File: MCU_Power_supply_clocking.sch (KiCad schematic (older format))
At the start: 111 parts, among them U6 STM32H743ZIT6, Y2 NX5032GA-8MHz, Y3 NX3215SA-32.768K-STD-MUA-14

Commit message: Buttons complete
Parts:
- added R?: 47, Resistor_SMD:R_0805_2012Metric_Pad1.20x1.40mm_HandSolder, symbol Device:R
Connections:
- net VDDA: now also R?.2; no longer JP1.1 (A), JP1.1 (A)
- new net: JP1.1 (A), JP1.1 (A), R?.1
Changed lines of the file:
@@
 $Descr A4 11693 8268
 encoding utf-8
-Sheet 5 9
+Sheet 5 10
 Title "Power_and_MCU_clock"
 Date "2021-04-29"
@@
 $EndComp
 Wire Wire Line
-	7680 4080 7890 4080
+	7380 4080 7590 4080
 Wire Wire Line
 	8500 4080 8290 4080
-Text Label 7680 4080 0    50   ~ 0
+Text Label 7380 4080 0    50   ~ 0
 VDDA
 Text Label 8500 4080 2    50   ~ 0
@@
 	1    0    0    -1
 $EndComp
-Text Label 7680 4080 0    50   ~ 0
+Text Label 7380 4080 0    50   ~ 0
 VDDA
 Text Label 8500 4080 2    50   ~ 0
@@
 Wire Wire Line
 	9010 3240 9010 3200
+$Comp
+L Device:R R?
+U 1 1 60D1EBF4
+P 7740 4080
+AR Path="/60D1EBF4" Ref="R?"  Part="1"
+AR Path="/60A03F8A/60D1EBF4" Ref="R?"  Part="1"
+F 0 "R?" V 7650 4080 50  0000 C CNN
+F 1 "47" V 7830 4080 50  0000 C CNN
+F 2 "Resistor_SMD:R_0805_2012Metric_Pad1.20x1.40mm_HandSolder" V 7670 4080 50  0001 C CNN
+F 3 "~" H 7740 4080 50  0001 C CNN
+	1    7740 4080
+	0    1    1    0
+$EndComp
 $EndSCHEMATC

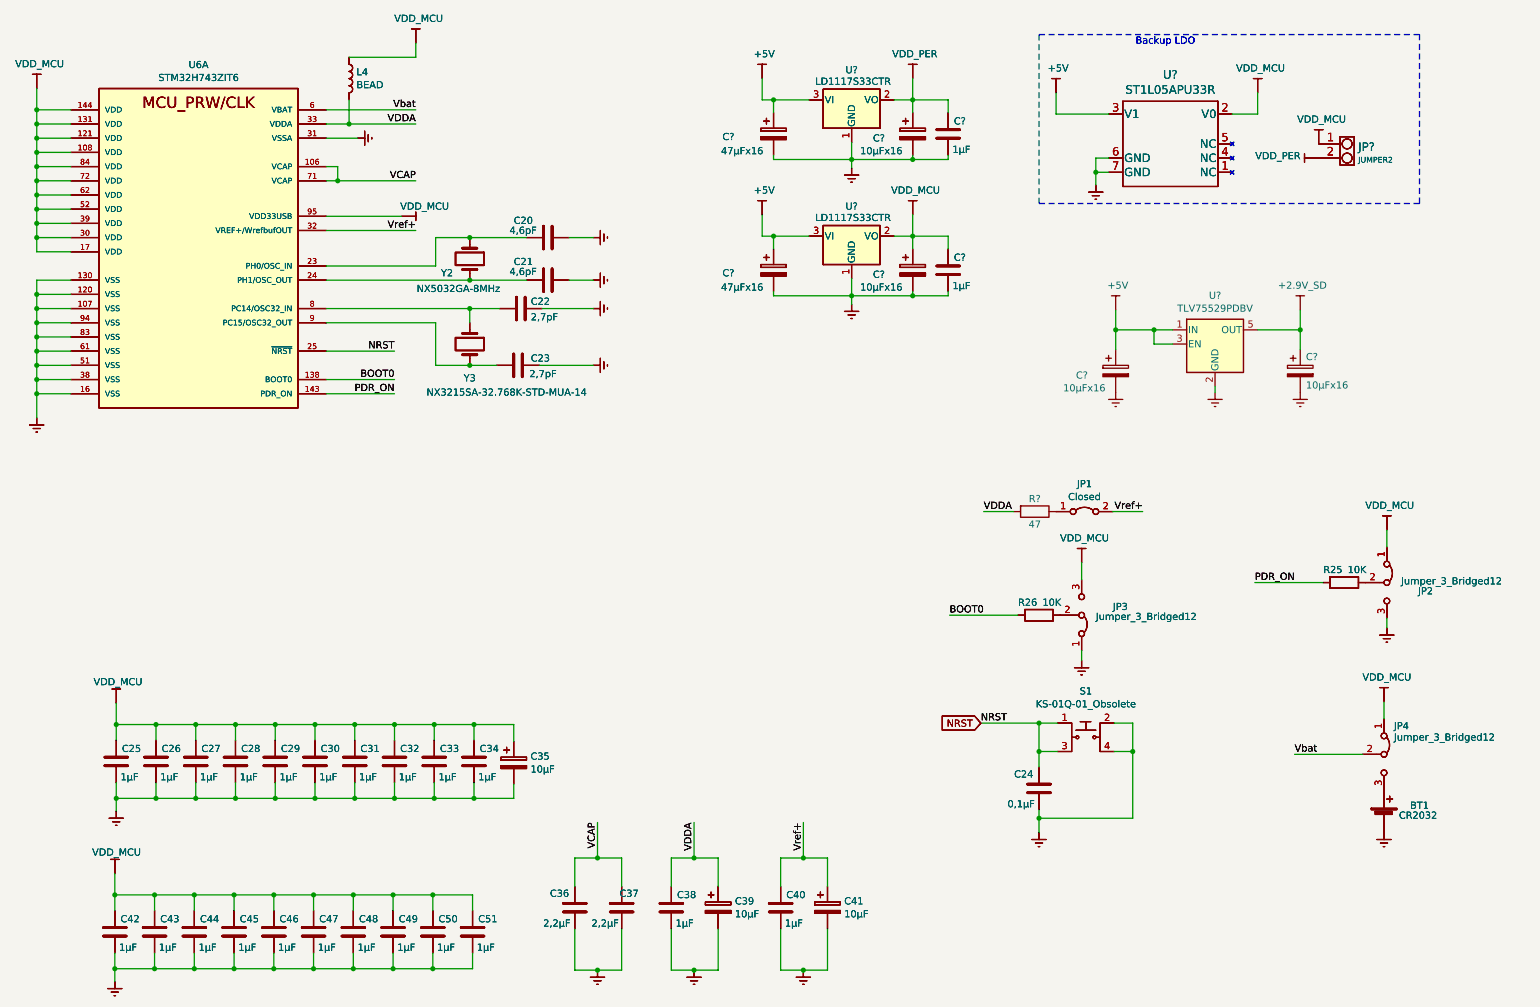
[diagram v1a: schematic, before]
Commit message: delete Main power scheet
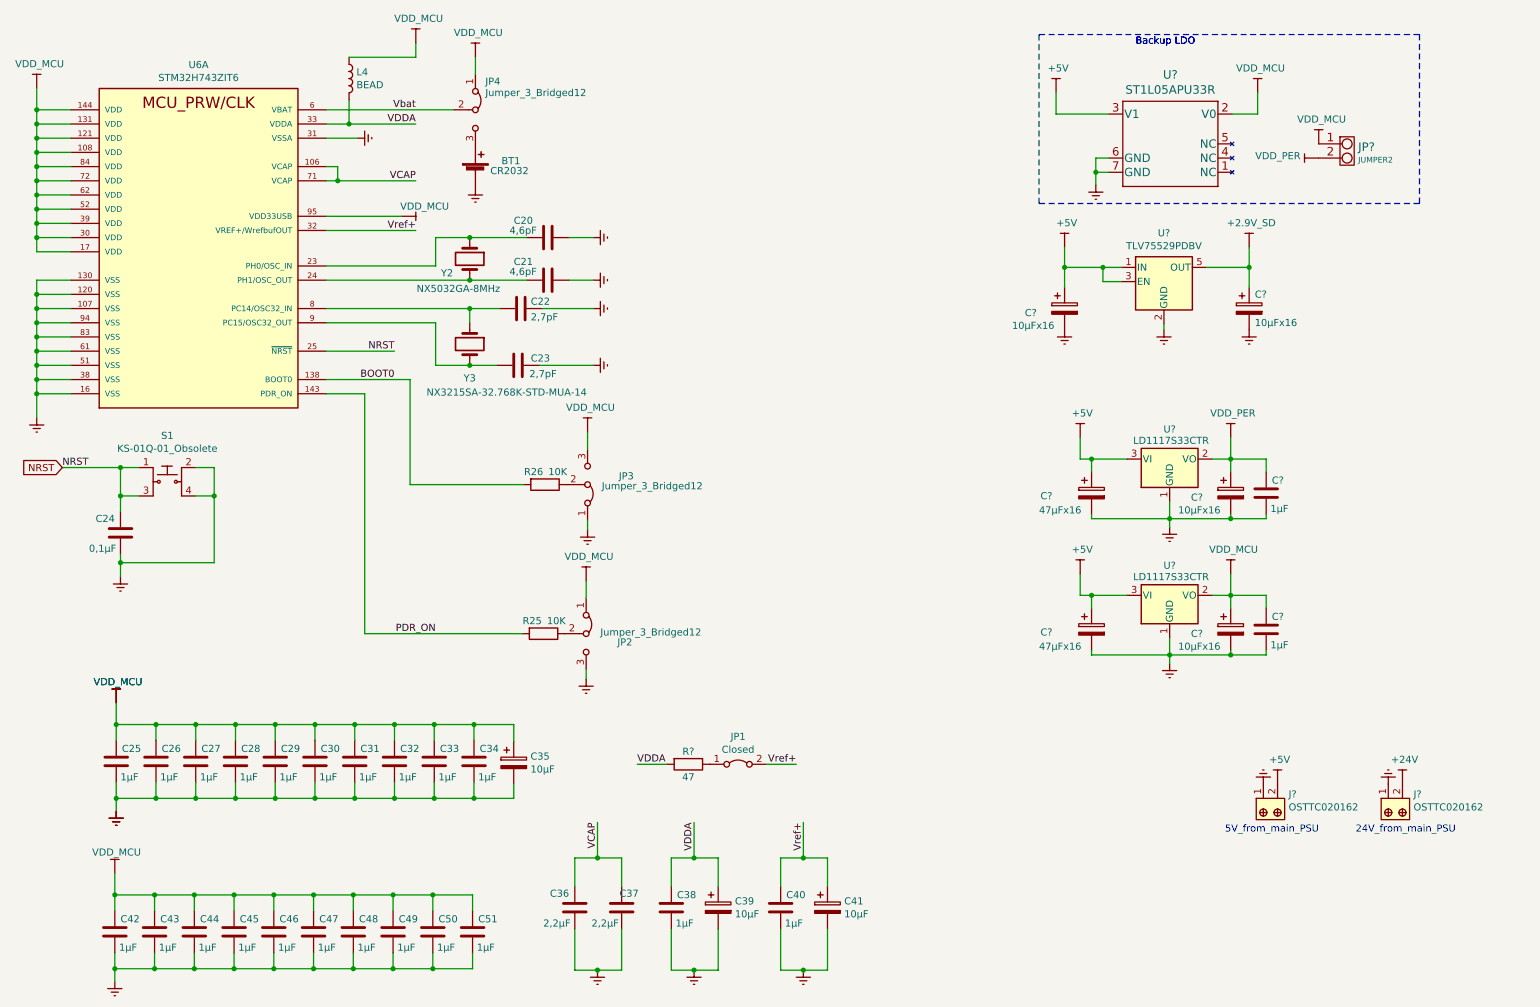
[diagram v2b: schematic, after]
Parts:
- removed BT1: CR2032, symbol Device:Battery_Cell
- removed C20, C21: 4,6pF, Capacitor_SMD:C_0603_1608Metric_Pad1.08x0.95mm_HandSolder, symbol Device:C
- removed C22, C23: 2,7pF, Capacitor_SMD:C_0603_1608Metric_Pad1.08x0.95mm_HandSolder, symbol Device:C
- removed C24: 0,1µF, Capacitor_SMD:C_0805_2012Metric_Pad1.18x1.45mm_HandSolder, symbol Device:C
- removed C25, C26, C27, C28, C29, C30, C31, C32, C33, C34, C38, C40, C42, C43, C44, C45, C46, C47, C48, C49, C50, C51, C? (x2): 1µF, Capacitor_SMD:C_0603_1608Metric_Pad1.08x0.95mm_HandSolder, symbol Device:C
- removed C35, C39, C41: 10µF, Capacitor_Tantalum_SMD:CP_EIA-3216-10_Kemet-I, symbol Device:CP
- removed C36, C37: 2,2µF, Capacitor_SMD:C_0805_2012Metric_Pad1.18x1.45mm_HandSolder, symbol Device:C
- removed C? (x2): 47µFx16, Capacitor_Tantalum_SMD:CP_EIA-7343-31_Kemet-D_Pad2.25x2.55mm_HandSolder, symbol Device:CP
- removed C? (x2): 10µFx16, symbol Device:CP
- removed JP1: Closed, symbol Jumper:Jumper_2_Bridged
- removed JP2, JP3, JP4: Jumper_3_Bridged12, symbol Jumper:Jumper_3_Bridged12
- removed JP?: JUMPER2, symbol freetronics_schematic:JUMPER2
- removed L4: BEAD, symbol Device:L
- removed R25, R26: 10K, Resistor_SMD:R_0805_2012Metric_Pad1.20x1.40mm_HandSolder, symbol Device:R
- removed S1: KS-01Q-01_Obsolete, digikey-footprints:PushButton_Round_D12mm_THT_KS-01Q-01, symbol dk_Pushbutton-Switches:KS-01Q-01_Obsolete
- removed U6: STM32H743ZIT6, QFP50P2200X2200X160-144N, symbol SVIELCOM_Library:STM32H743ZIT6
- removed U? (x2): LD1117S33CTR, Package_TO_SOT_SMD:SOT-223-3_TabPin2, symbol Regulator_Linear:LD1117S33TR_SOT223
- removed U?: ST1L05APU33R, DFN_5APU33R_STM, symbol SVIELCOM_Library:ST1L05APU33R
- removed Y2: NX5032GA-8MHz, Crystal:Crystal_SMD_5032-2Pin_5.0x3.2mm_HandSoldering, symbol Device:Crystal
- removed Y3: NX3215SA-32.768K-STD-MUA-14, Crystal:Crystal_SMD_MicroCrystal_CC7V-T1A-2Pin_3.2x1.5mm_HandSoldering, symbol Device:Crystal
- added J? (x2): OSTTC020162, digikey-footprints:Term_Block_1x2_P5mm, symbol dk_Terminal-Blocks-Wire-to-Board:OSTTC020162
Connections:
- net +5V: now also J?.2
- net GNDREF: now also J?.1, J?.1
- new net +24V: J?.2
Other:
- note added: "24V_from_main_PSU"
- note added: "5V_from_main_PSU"
- moved on the sheet: BT1, C24, C?, JP1, JP2, JP3, JP4, R25, R26, R?, S1, U?

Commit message: v0.1
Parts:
- gave numbers to parts that had none: 16
- renumbered C20 to C10, C21 to C11, C22 to C12, C23 to C15, C24 to C19, C25 to C23, C26 to C24, C27 to C25, C28 to C26, C29 to C27, C30 to C28, C31 to C29, C32 to C30, C33 to C31, C34 to C32, C35 to C33, C36 to C34, C37 to C35, C38 to C36, C39 to C37, C40 to C38, C41 to C39, C42 to C40, C43 to C41, C44 to C42, C45 to C43, C46 to C44, C47 to C45, C48 to C46, C49 to C47, C50 to C48, C51 to C49, JP4 to JP1, JP2 to JP4, JP1 to JP5, L4 to L2, R26 to R14, R25 to R15, U6 to U11, Y2 to Y1, Y3 to Y2
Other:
- moved on the sheet: J2, J3

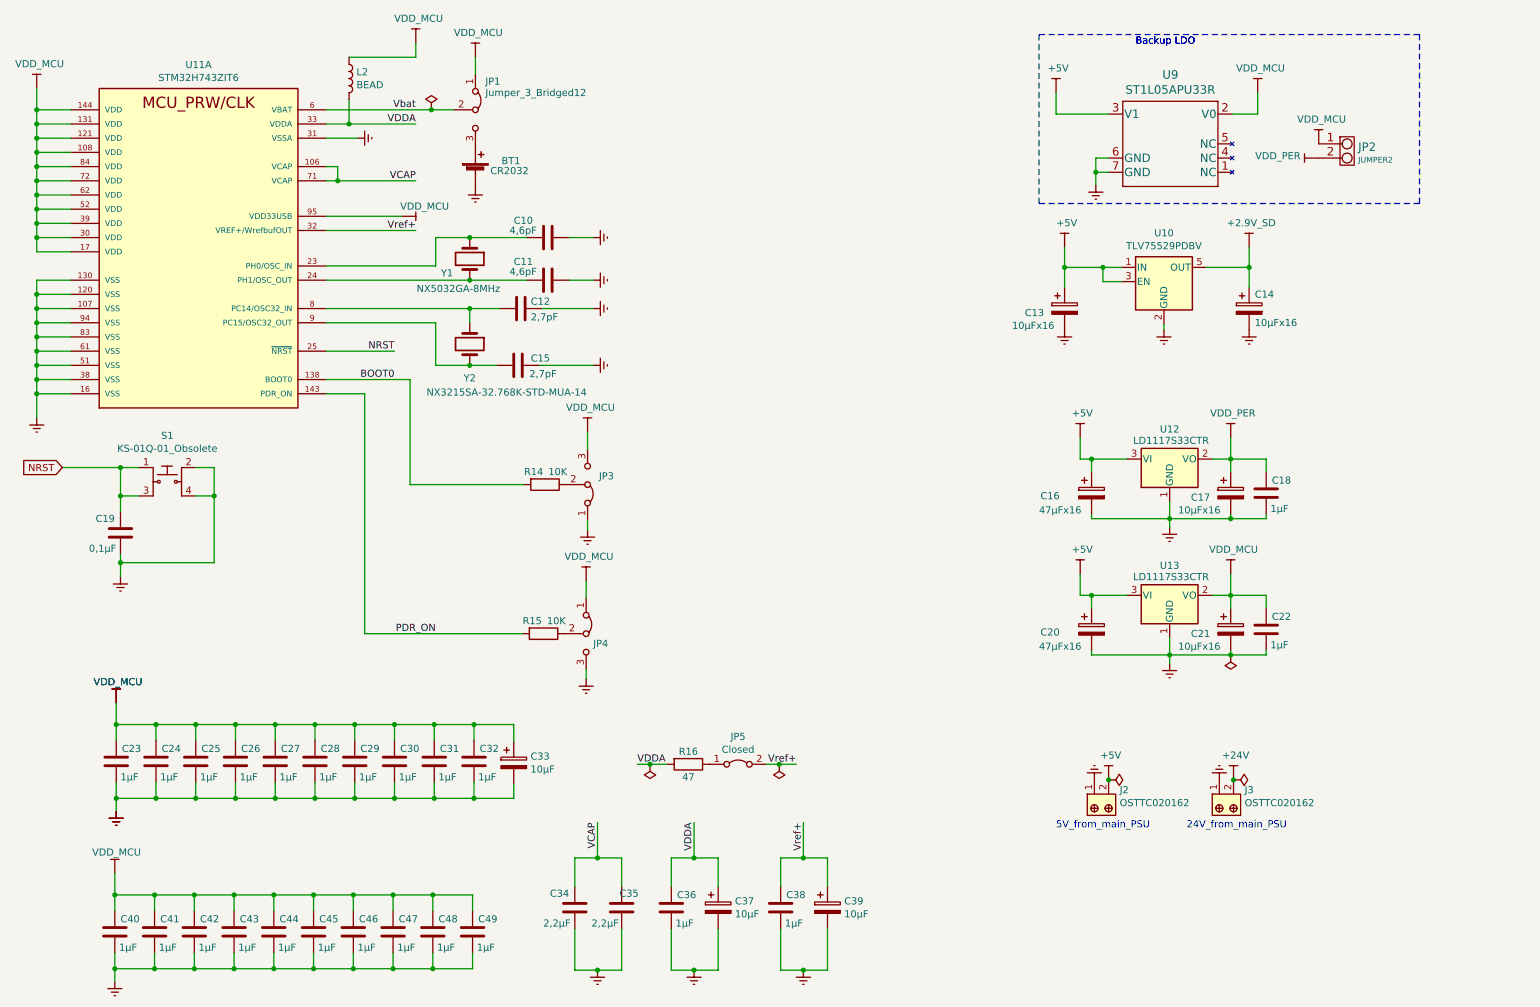
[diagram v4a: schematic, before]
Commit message: v0.3 changed sd_card holder
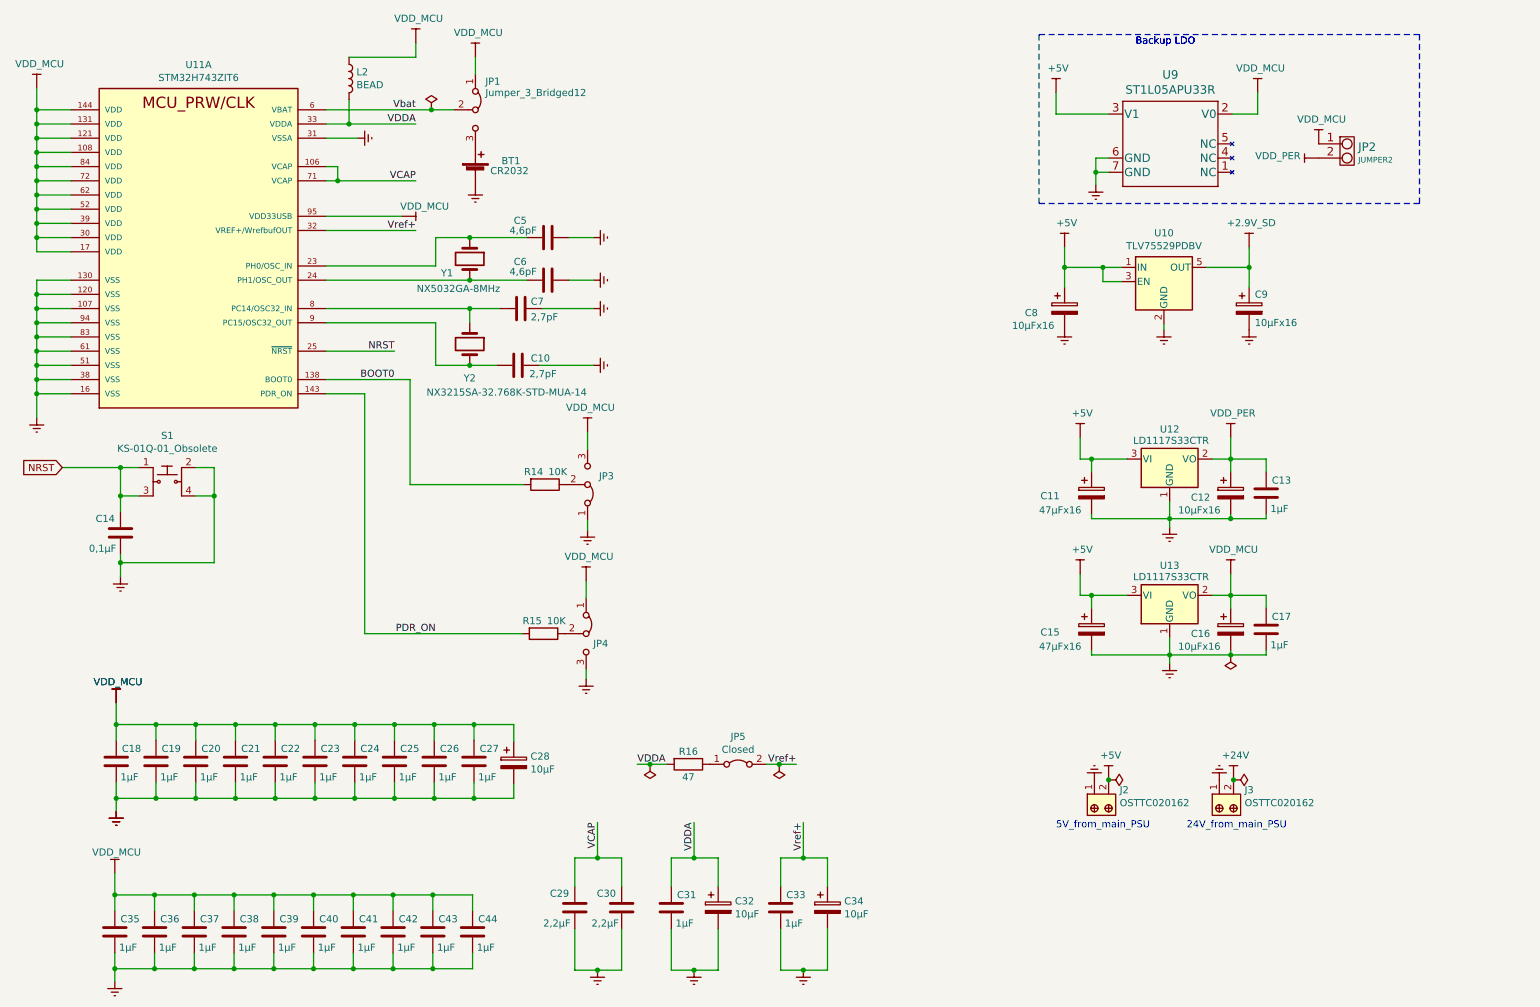
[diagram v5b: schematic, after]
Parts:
- BT1: footprint (none) -> SVIELCOM:BAT_BS-7
- C12: renamed from C17; footprint (none) -> Capacitor_Tantalum_SMD:CP_EIA-3216-10_Kemet-I
- C14: renamed from C19; footprint Capacitor_SMD:C_0805_2012Metric_Pad1.18x1.45mm_HandSolder -> Capacitor_SMD:C_0603_1608Metric_Pad1.08x0.95mm_HandSolder
- C16: renamed from C21; footprint (none) -> Capacitor_Tantalum_SMD:CP_EIA-3216-10_Kemet-I
- C29: renamed from C34; Type (none) -> C2012X7R1H225KT000E
- C30: renamed from C35; Type (none) -> C2012X7R1H225KT000E
- C8: renamed from C13; footprint (none) -> Capacitor_Tantalum_SMD:CP_EIA-3216-10_Kemet-I
- C9: renamed from C14; footprint (none) -> Capacitor_Tantalum_SMD:CP_EIA-3216-10_Kemet-I
- renumbered C15 to C10, C16 to C11, C18 to C13, C20 to C15, C22 to C17, C23 to C18, C24 to C19, C25 to C20, C26 to C21, C27 to C22, C28 to C23, C29 to C24, C30 to C25, C31 to C26, C32 to C27, C33 to C28, C36 to C31, C37 to C32, C38 to C33, C39 to C34, C40 to C35, C41 to C36, C42 to C37, C43 to C38, C44 to C39, C45 to C40, C46 to C41, C47 to C42, C48 to C43, C49 to C44, C10 to C5, C11 to C6, C12 to C7
